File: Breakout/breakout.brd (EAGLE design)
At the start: 52.5 x 42.5 mm, 57 parts, among them Q1 16Mhz, U1 TPS63001DRCT, U11 XL

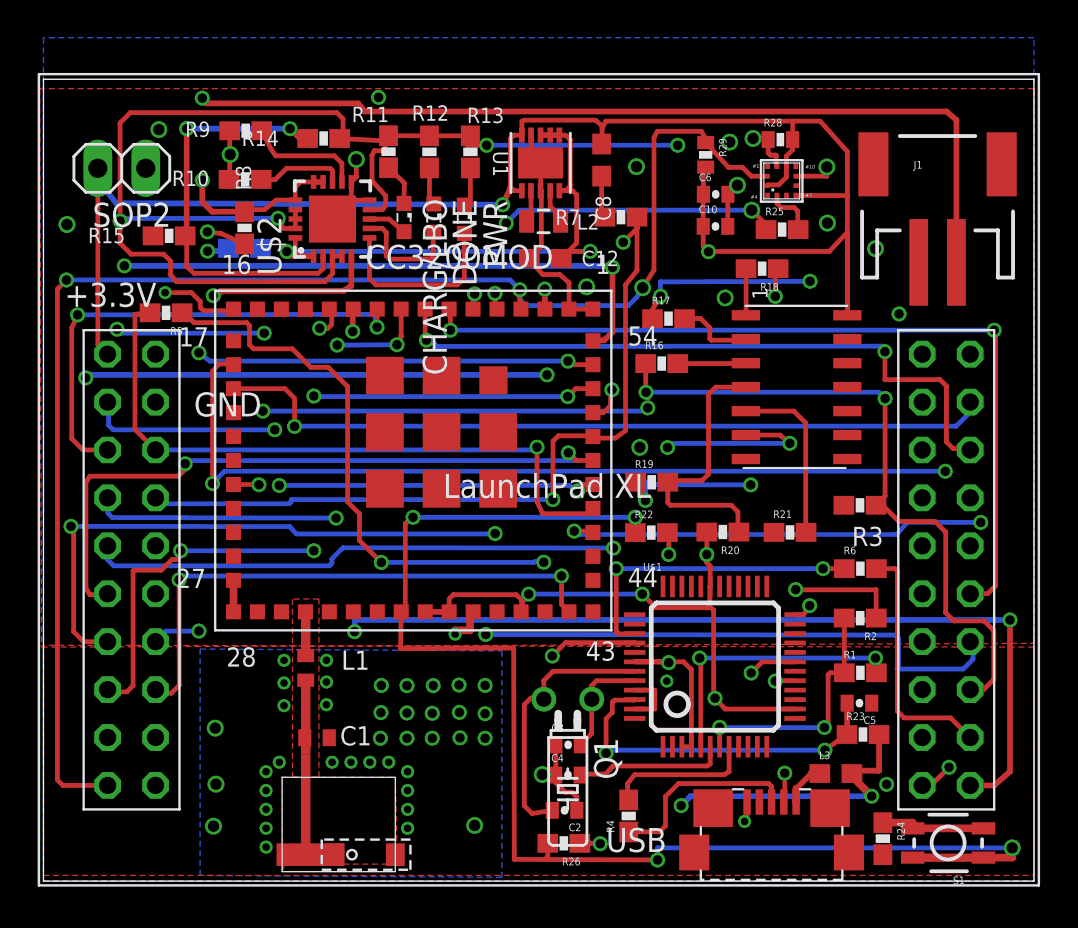
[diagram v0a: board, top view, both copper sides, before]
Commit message: Added EEPROM for FTDI chip
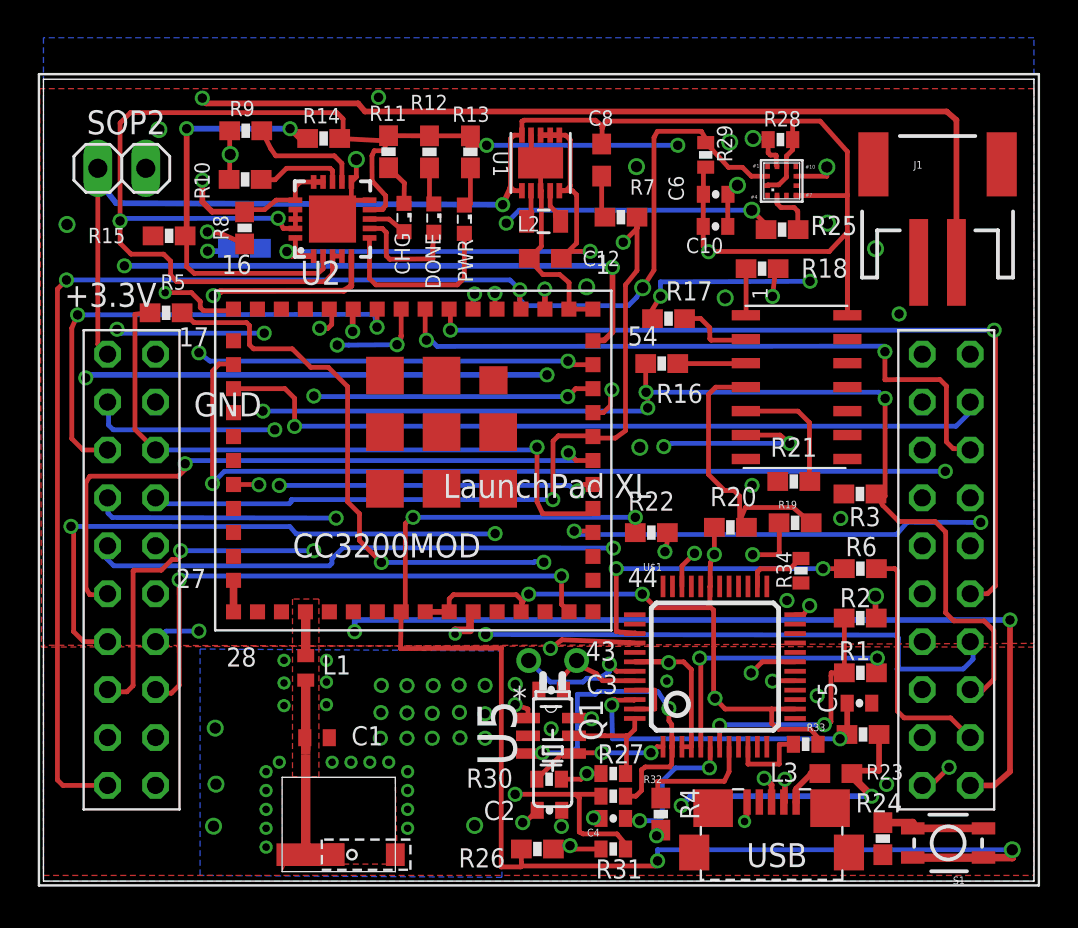
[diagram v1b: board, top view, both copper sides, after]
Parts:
- added R27, R30, R31, R33, R34: 10K, SparkFun-Passives:0402-RES
- added R32: 2.2K, SparkFun-Passives:0402-RES
- added U5: 93LC46BT-I/OT, Microchip_By_element14_Batch_1:SOT95P280X145-6N
- moved R19 7.90 mm to (51.8, 19.0)
- moved C4 3.32 mm to (42.2, 3.32)
- moved C3 3.04 mm to (38.9, 10.1)
- moved R21 2.71 mm to (51.8, 21.2)
- moved Q1 2.20 mm to (39.0, 11.7)
- moved R4 1.70 mm to (44.7, 3.55)
- moved R26 1.43 mm to (38.2, 1.70)
- moved C2 0.80 mm to (38.8, 3.75)
- moved R3 0.60 mm to (55.3, 20.5)
- moved R20 0.47 mm to (48.4, 18.8)
- renumbered CHARG/LBO to CHG, U$2 to U2
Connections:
- new net N$16: R4.1, USB.2
- new net N$24: R2.1, USB.3
- new net N$54: R31.1, R32.2, U5.1
- new net N$55: R33.2, U$1.10
- new net N$56: R34.2, U$1.26
- net GND: now also U5.2
- net N$39: now also R27.1, U$1.48, U5.5; no longer USB.4
- net N$41: now also R30.1, U$1.1, U5.4; no longer R4.1, USB.3
- net N$42: now also R32.1, U$1.2, U5.3; no longer R2.1, USB.2
- net VCC: now also R27.2, R30.2, R31.2, R33.1, U5.6
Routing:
- net N$24: track 0.00 -> 18.2 mm, vias 0 -> 2
- net N$54: track 0.00 -> 15.6 mm, vias 0 -> 2
- net VCC: track 152.3 -> 167.6 mm, vias 7 -> 9
- net N$16: track 0.00 -> 11.8 mm, vias 0 -> 2
- net N$47: track 20.4 -> 12.0 mm, vias 3 -> 2
- net N$39: track 0.00 -> 5.96 mm
- net N$55: track 0.00 -> 4.38 mm
- net N$56: track 0.00 -> 3.36 mm
- net N$41: track 10.4 -> 7.40 mm, vias 0 -> 2
- net N$38: track 14.2 -> 16.6 mm, vias 0 -> 2
- net N$49: track 9.25 -> 6.91 mm
- net GND: track 45.0 -> 42.9 mm, vias 58 -> 66
- net USB_DM: track 7.87 -> 6.45 mm
- net DBG_RST_N: track 14.8 -> 15.9 mm
- net N$51: track 18.9 -> 18.3 mm
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
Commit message: Temp Sensor added
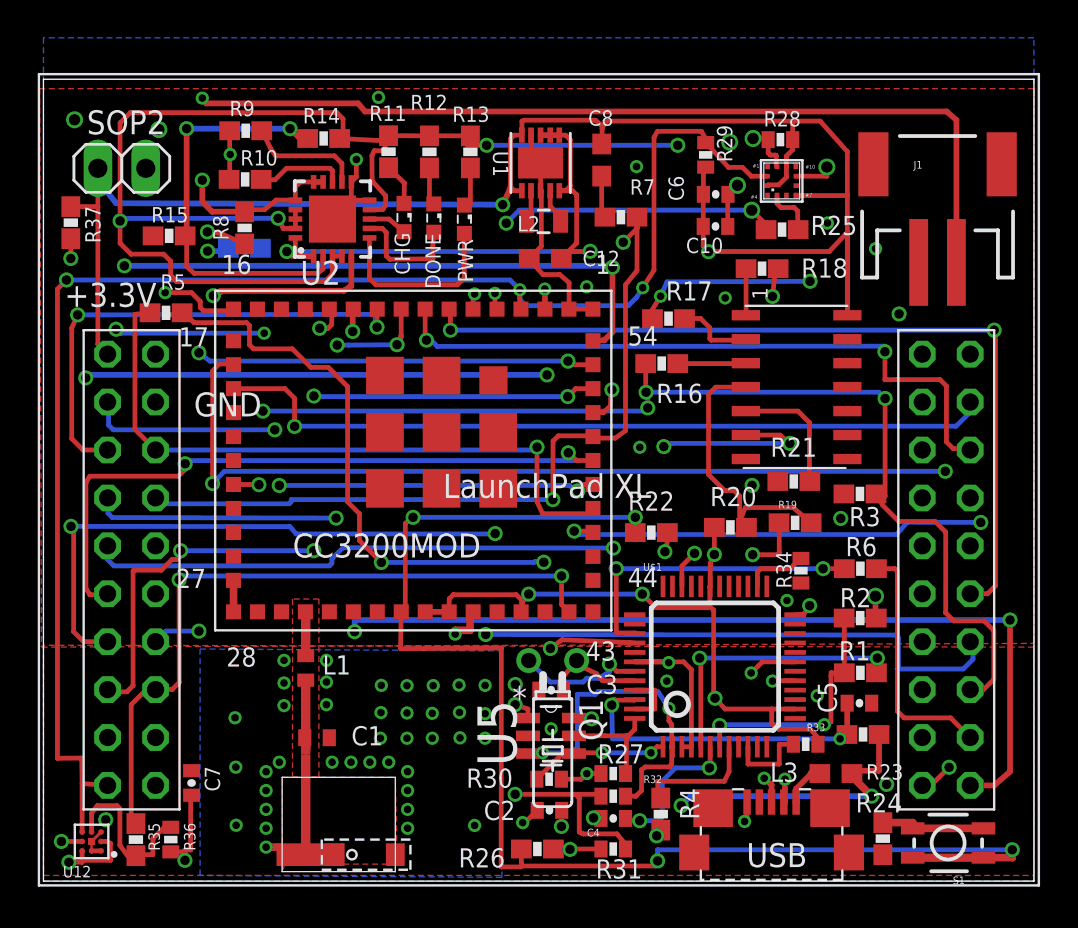
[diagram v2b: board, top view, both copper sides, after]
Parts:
- added C7: .1uF, SparkFun-Capacitors:0402-CAP
- added R35, R37: 0R, SparkFun-Passives:0603-RES
- added R36: 33K, SparkFun-Passives:0402-RES
- added U12: TMP006, SparkFun-DigitalIC:BGA8DS
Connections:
- new net GPIO_30: CC3200MOD.P42, R35.1, U11.GPIO_30
- new net N$57: R35.2, R36.1, U12.C2
- net GND: now also C7.1, U12.A1, U12.A2, U12.C1
- net GPIO_10: now also U12.B3
- net GPIO_11: now also U12.C3
- net N$14: now also C7.2, R36.2, R37.2, U12.A3, U12.B1; no longer CC3200MOD.P42, U11.GPIO_30
- net VCC: now also R37.1
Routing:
- net GPIO_30: track 0.00 -> 37.7 mm, vias 0 -> 2
- net N$14: track 29.6 -> 52.2 mm, vias 2 -> 3
- net N$57: track 0.00 -> 8.91 mm
- net GPIO_10: track 76.2 -> 84.0 mm, vias 4 -> 5
- net GPIO_11: track 77.9 -> 80.6 mm
- net GND: track 42.9 -> 45.2 mm, vias 66 -> 67
- net VCC: track 167.6 -> 168.9 mm
